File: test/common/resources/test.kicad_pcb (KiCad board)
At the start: 2 copper layers, 3 parts

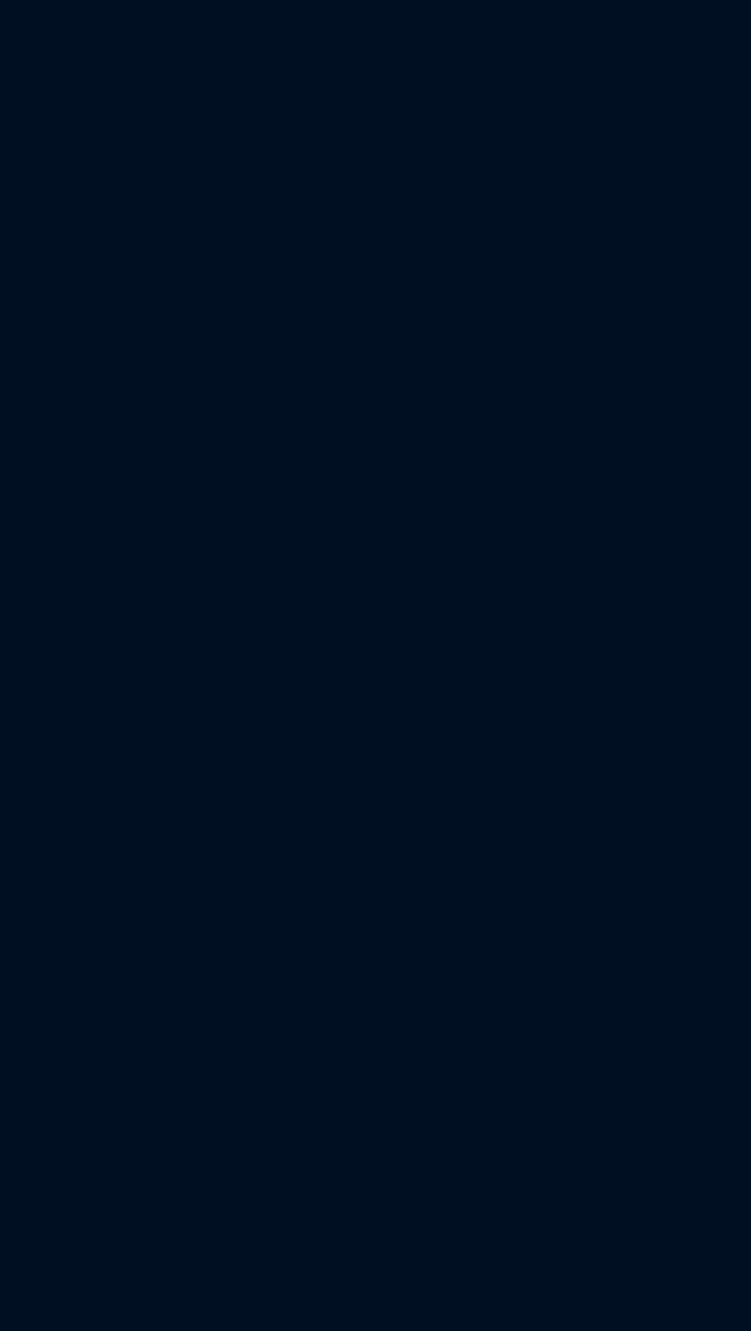
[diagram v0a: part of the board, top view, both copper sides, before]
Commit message: Fileformat: Add order & fix enums & add test cases
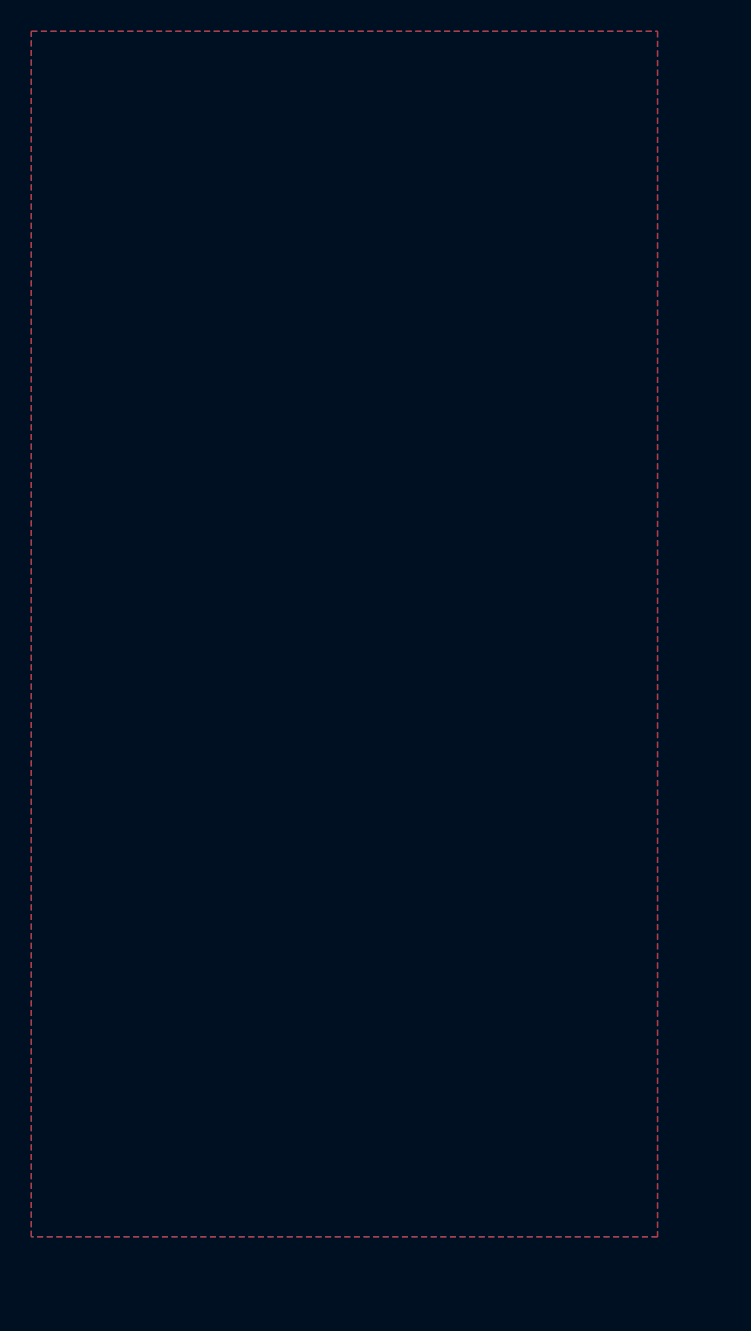
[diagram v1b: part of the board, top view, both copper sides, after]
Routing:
- added copper zone on B.Cu, net GND
- added copper zone on F.Cu, net GND
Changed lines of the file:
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@@
         (58 "User.9" user))
     (setup
+        (stackup
+            (layer "F.SilkS"
+                (type "Top Silk Screen")
+            )
+            (layer "F.Paste"
+                (type "Top Solder Paste")
+            )
+            (layer "F.Mask"
+                (type "Top Solder Mask")
+                (color "Green")
+                (thickness 0.01524)
+                (material "Epoxy")
+                (epsilon_r 3.8)
+                (loss_tangent 0)
+            )
+            (layer "F.Cu"
+                (type "copper")
+                (thickness 0.035)
+            )
+            (layer "dielectric 1"
+                (type "prepreg")
+                (color "FR4 natural")
+                (thickness 0.0994)
+                (material "FR4")
+                (epsilon_r 4.1)
+                (loss_tangent 0.02)
+            )
+            (layer "In1.Cu"
+                (type "copper")
+                (thickness 0.0152)
+            )
+            (layer "dielectric 2"
+                (type "core")
+                (color "FR4 natural")
+                (thickness 1.24)
+                (material "FR4")
+                (epsilon_r 4.43)
+                (loss_tangent 0.02)
+            )
+            (layer "In2.Cu"
+                (type "copper")
+                (thickness 0.0152)
+            )
+            (layer "dielectric 3"
+                (type "prepreg")
+                (color "FR4 natural")
+                (thickness 0.0994)
+                (material "FR4")
+                (epsilon_r 4.1)
+                (loss_tangent 0.02)
+            )
+            (layer "B.Cu"
+                (type "copper")
+                (thickness 0.035)
+            )
+            (layer "B.Mask"
+                (type "Bottom Solder Mask")
+                (color "Green")
+                (thickness 0.01524)
+                (material "Epoxy")
+                (epsilon_r 3.8)
+                (loss_tangent 0)
+            )
+            (layer "B.Paste"
+                (type "Bottom Solder Paste")
+            )
+            (layer "B.SilkS"
+                (type "Bottom Silk Screen")
+            )
+            (copper_finish "HAL SnPb")
+            (dielectric_constraints yes))
         (pad_to_mask_clearance 0)
         (allow_soldermask_bridges_in_footprints no)
@@
             (drillshape 1)
             (scaleselection 1)
-            (outputdirectory "")))
+            (outputdirectory ""))
+        )
     (net 0 "")
     (net 1 "B1-1-R1-2")
@@
                 (xyz 1 1 1))
             (rotate
-                (xyz 0 0 0)))))
+                (xyz 0 0 0))))
+    (zone
+		(net 2)
+		(net_name "GND")
+		(layers "F.Cu" "In1.Cu" "In2.Cu" "B.Cu")
+		(name "layer_fill_GND")
+		(hatch edge 0.5)
+		(connect_pads
+			(clearance 0.2)
+		)
+		(min_thickness 0.2)
+		(filled_areas_thickness no)
+		(fill yes
+			(thermal_gap 0.2)
+			(thermal_bridge_width 0.2)
+			(island_removal_mode 2)
+			(island_area_min 10)
+		)
+		(polygon
+			(pts
+				(xy -20 -1) (xy 20 -1) (xy 20 76) (xy -20 76)
+			)
+		)))
